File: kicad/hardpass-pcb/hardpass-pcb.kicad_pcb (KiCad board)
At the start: 2 copper layers, 30 x 65 mm, 27 parts, among them CON1 ER-OLED-FPC20, P1 Pi_Zero, SW1 1, SW10 C/UP, SW11 0/OK, SW12 OK/DN, SW2 2, SW3 3, SW4 4, SW5 5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

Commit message: added reset circuit to oled
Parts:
- added C7: 0.1µF, Capacitors_SMD:C_1206, B.Cu at (134.5, 88.2)
- added R2: 100k, Resistors_SMD:R_1206, B.Cu at (141.0, 88.2)
- added R3: 100k, Resistors_SMD:R_1206, B.Cu at (137.8, 88.2)
- moved C1 0.11 mm to (130.8, 104.0), turned to 270 degrees
- moved C2 0.11 mm to (146.2, 101.5), turned to 180 degrees
- moved R10 0.11 mm to (137.8, 93.5), turned to 90 degrees
- moved R11 0.10 mm to (141.0, 93.5), turned to 90 degrees
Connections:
- net Net-(CON1-Pad10) renamed /OLED_CS
- net Net-(CON1-Pad12) renamed /OLED_DC
- C1 pad 1: +3V3 -> GND
- C1 pad 2: GND -> +3V3
- C2 pad 1: +3V3 -> GND
- C2 pad 2: GND -> +3V3
- CON1 pad 11: Net-(CON1-Pad11) -> /OLED_RES
- R10 pad 1: +3V3 -> OLED_SCL
- R10 pad 2: OLED_SCL -> +3V3
- R11 pad 1: +3V3 -> OLED_SDA
- R11 pad 2: OLED_SDA -> +3V3
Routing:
- net /OLED_RES: track 0.00 -> 12.6 mm, vias 0 -> 2
- net Net-(C7-Pad1): track 0.00 -> 6.59 mm
- net +3V3: track 39.4 -> 39.5 mm, vias 6 -> 7

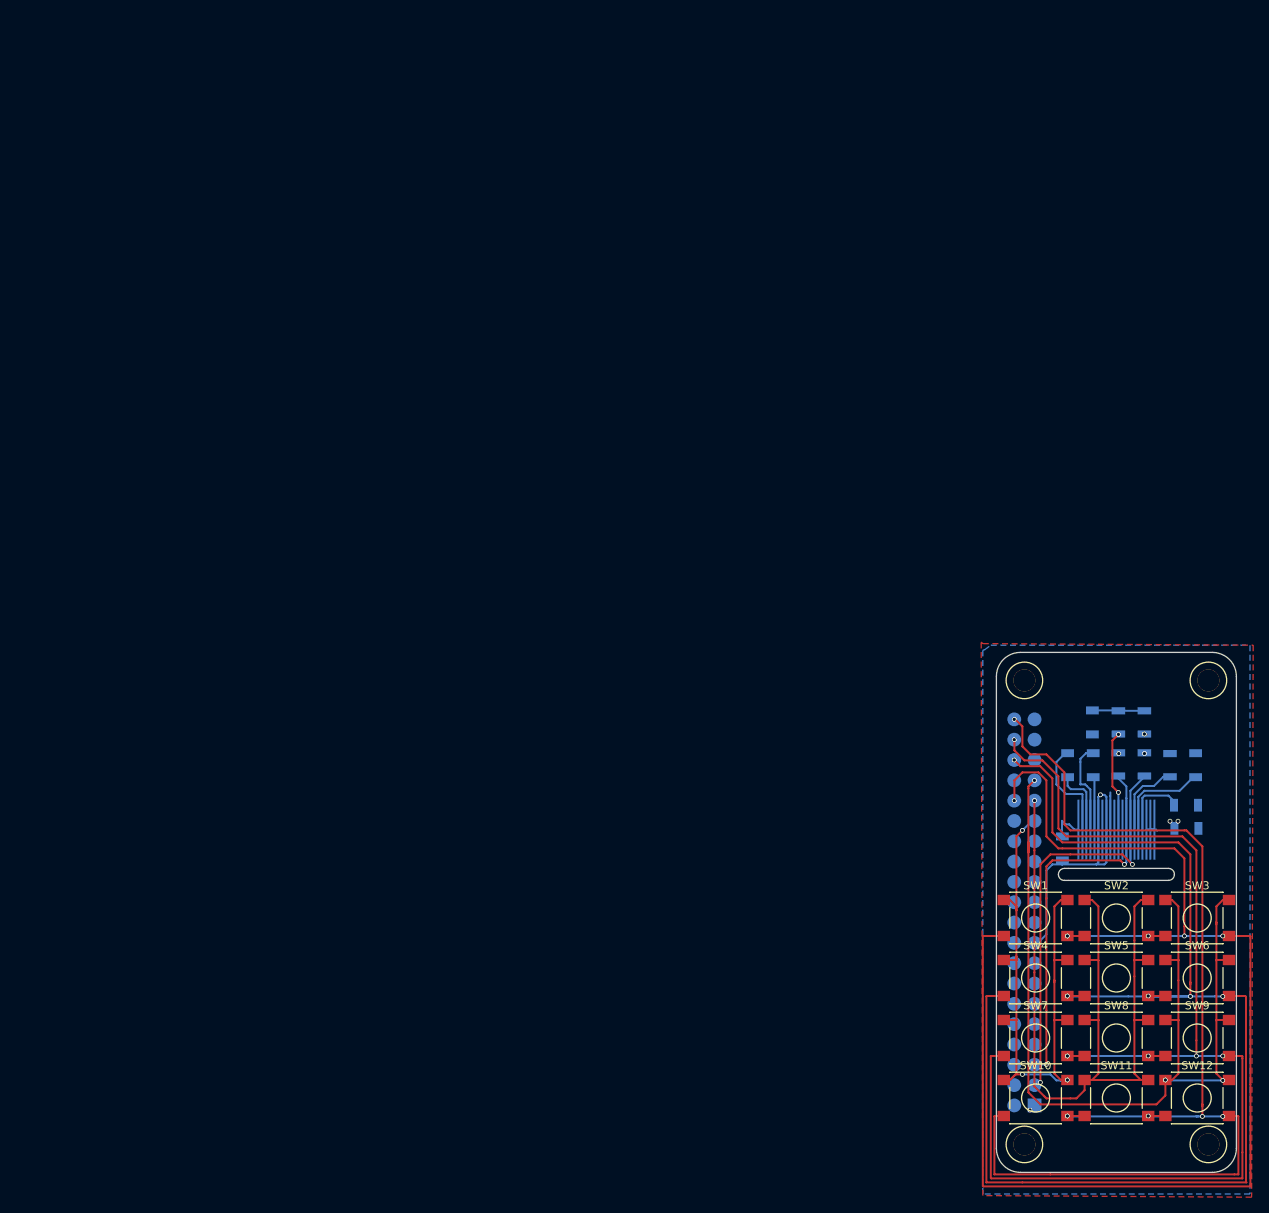
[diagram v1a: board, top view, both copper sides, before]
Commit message: re-done pcb for 30 pin oled
pcb was completely redone, fixing header-misalignment (hopefully) and removing ugly silk screen from the front
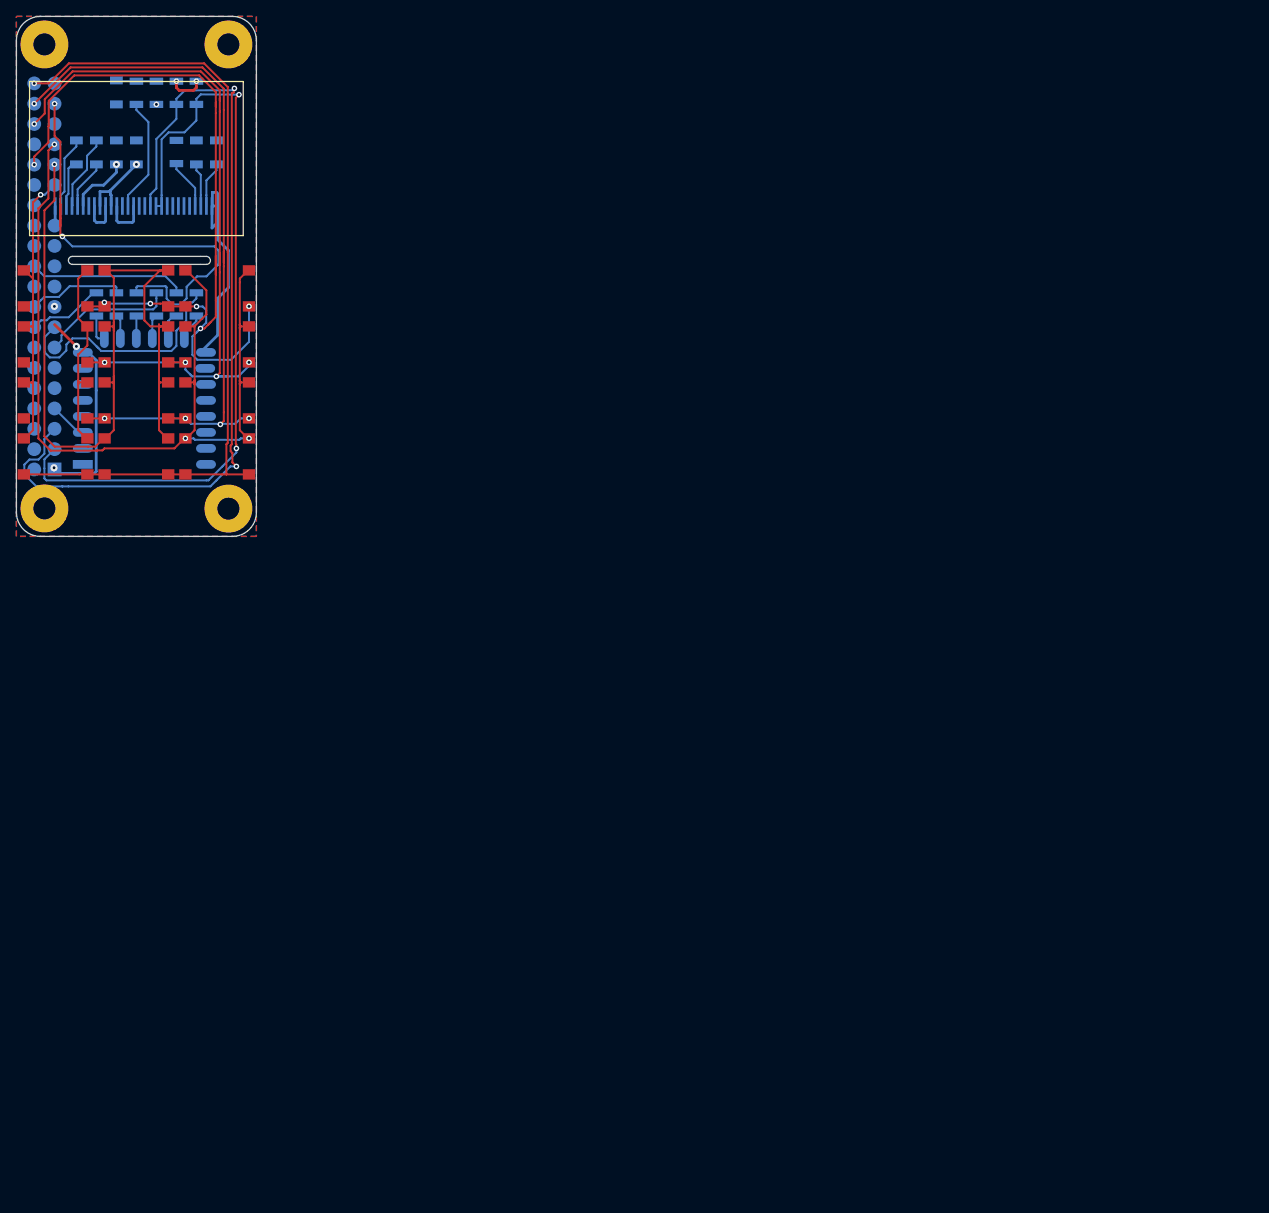
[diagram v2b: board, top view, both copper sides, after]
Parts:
- removed CON1: ER-OLED-FPC20, hardpass:Solderpads_OLED20Pin_.5mmPitch
- removed the REF** at (126.0, 83.0)
- removed the REF** at (149.0, 141.0)
- removed the REF** at (126.0, 141.0)
- removed the REF** at (149.0, 83.0)
- added P2: OLED_I2C, adafruit-oled:UG-2864HSWEG01_0.96IN_WRAPAROUND, F.Cu at (15.0, 22.5)
- added R12: 33, Resistors_SMD:R_1206, B.Cu at (10.0, 36.0)
- added R13: 33, Resistors_SMD:R_1206, B.Cu at (12.5, 36.0)
- added R14: 33, Resistors_SMD:R_1206, B.Cu at (15.0, 36.0)
- added R15: 33, Resistors_SMD:R_1206, B.Cu at (17.5, 36.0)
- added R16: 33, Resistors_SMD:R_1206, B.Cu at (20.0, 36.0)
- added R17: 33, Resistors_SMD:R_1206, B.Cu at (22.5, 36.0)
- added REF**: 1pin, hardpass:1pin_nosilk, F.Cu at (26.5, 61.5)
- added REF**: 1pin, hardpass:1pin_nosilk, F.Cu at (3.50, 61.5)
- added REF**: 1pin, hardpass:1pin_nosilk, F.Cu at (26.5, 3.50)
- added REF**: 1pin, hardpass:1pin_nosilk, F.Cu at (3.50, 3.50)
- added U2: ESP-12E, hardpass:ESP-12E_smd, B.Cu at (9.00, 56.0)
- P1: footprint hardpass:Pin_Header_Mirrored-NoHoles_2x20 -> hardpass:Pin_Header_Mirrored-NoHoles_centered_2x20
- SW1, SW10, SW11, SW12, SW2, SW3, SW4, SW5, SW6, SW7, SW8, SW9: footprint Buttons_Switches_SMD:SW_SPST_PTS645 -> hardpass:SW_SPST_PTS645_nosilk
- moved P1 159.6 mm to (3.50, 32.5)
- moved C2 156.1 mm to (15.0, 17.0), turned to 270 degrees
- moved C1 146.8 mm to (12.5, 17.0)
- moved C4 146.5 mm to (22.5, 17.0)
- moved R2 146.4 mm to (17.5, 9.55)
- moved SW10 146.4 mm to (4.90, 55.0)
- moved SW11 146.4 mm to (15.0, 55.0)
- moved SW12 146.4 mm to (25.1, 55.0)
- moved C5 146.3 mm to (10.0, 17.0)
- moved SW7 146.1 mm to (4.90, 48.0)
- moved SW8 146.1 mm to (15.0, 48.0)
- moved SW9 146.1 mm to (25.1, 48.0)
- moved C3 146.1 mm to (25.0, 17.0), turned to 90 degrees
- moved R1 145.9 mm to (20.0, 16.9)
- moved SW4 145.9 mm to (4.90, 41.0)
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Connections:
- R3 pad 1: /OLED_RES -> Net-(P2-Pad14)
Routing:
- net ROW_2: track 162.1 -> 92.1 mm
- net ROW_1: track 167.8 -> 101.6 mm, vias 5 -> 6
- net OLED_SCL: track 48.1 -> 106.8 mm
- net SD_D2: track 0.00 -> 57.4 mm, vias 0 -> 2
- net ROW_3: track 148.2 -> 93.4 mm
- net OLED_SDA: track 52.4 -> 97.4 mm
- net ROW_4: track 141.6 -> 103.6 mm, vias 5 -> 1
- net ESP_CLK: track 0.00 -> 30.9 mm
- net GND: track 12.1 -> 42.0 mm
- net SD_D1: track 0.00 -> 19.6 mm
- net SD_D3: track 0.00 -> 16.9 mm
- net Net-(P2-Pad14): track 0.00 -> 14.4 mm
- net COL_1: track 78.1 -> 64.5 mm, vias 3 -> 1
- net /OLED_RES: track 12.6 -> 0.00 mm, vias 2 -> 0
- net SD_D0: track 0.00 -> 12.1 mm
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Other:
- outline, holes or cut-outs redrawn
- net class Default: clearance 0.2 -> 0.25; via_dia 0.6 -> 0.7; via_drill 0.4 -> 0.35
- net class Power: clearance 0.2 -> 0.25; trace_width 0.45 -> 0.35; via_dia 0.6 -> 0.9; via_drill 0.4 -> 0.35
- rule pad_to_mask_clearance: 0.2 -> 0
- rule trace_clearance: 0.2 -> 0.25
- rule via_min_size: 0.4 -> 0.7

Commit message: added logo
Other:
- board text added: "hardpass 0.2.2"
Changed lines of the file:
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@@
     (links 107)
     (no_connects 7)
-    (area -0.050001 -0.050001 30.050001 65.050001)
+    (area -0.666014 -0.573 30.425001 65.655)
     (thickness 1.6)
-    (drawings 14)
+    (drawings 15)
     (tracks 547)
     (zones 0)
@@
       (net 1 GND))
   )
+  (gr_text "hardpass 0.2.2" (at 15 61.5) (layer F.SilkS)
+    (effects (font (size 1.5 1.5) (thickness 0.3)))
+  )
   (gr_line (start 23 30) (end 23.75 30) (layer Edge.Cuts) (width 0.1))

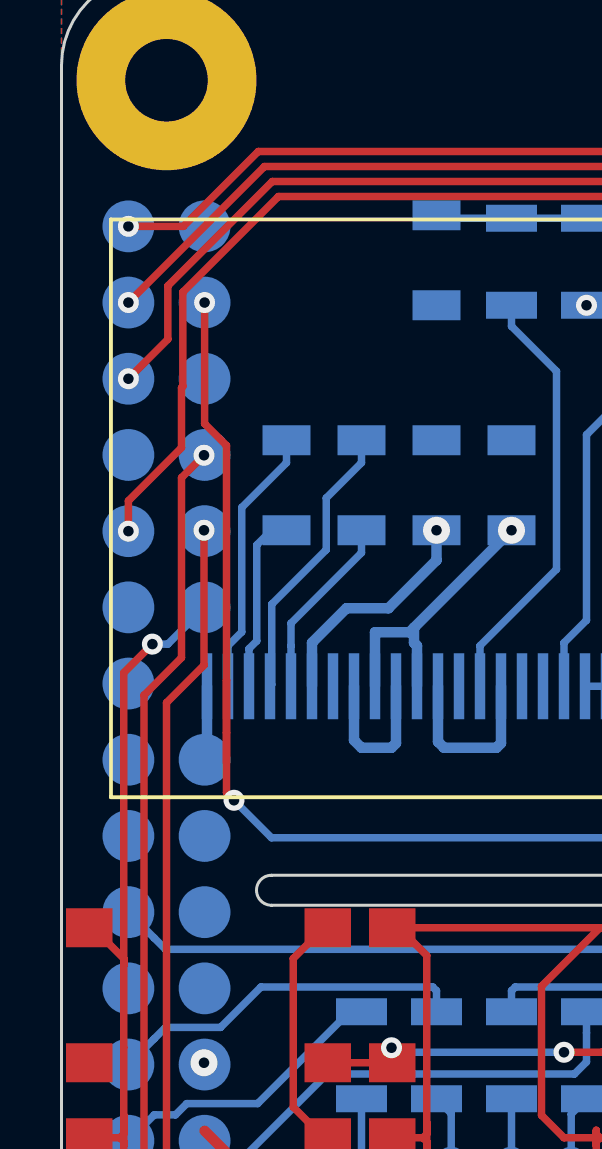
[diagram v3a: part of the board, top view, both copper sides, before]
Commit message: add tda8029 footprint
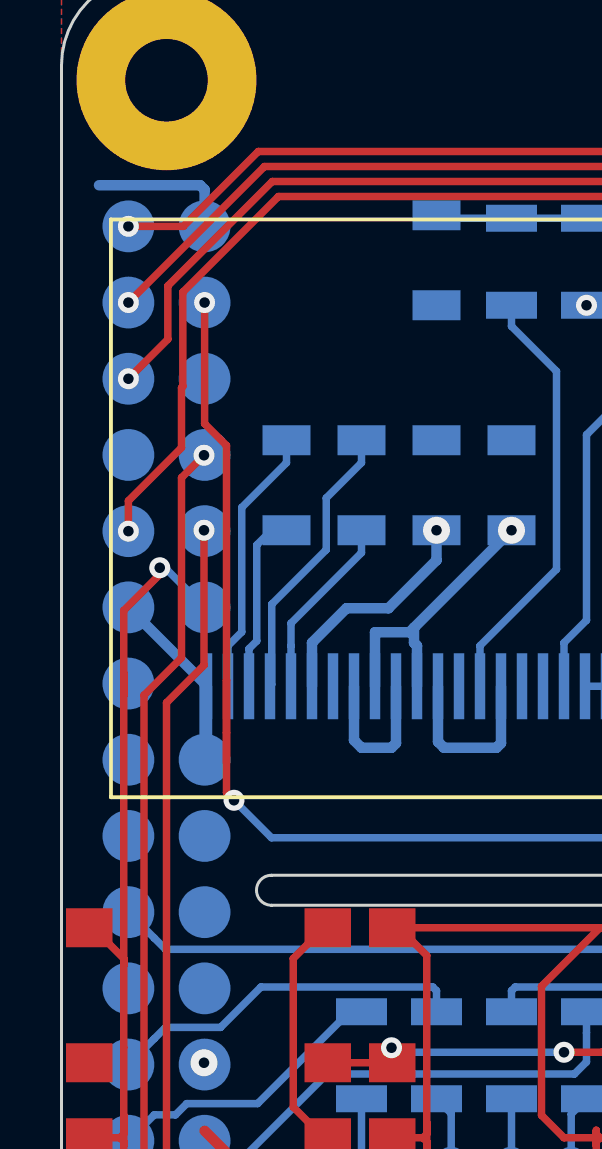
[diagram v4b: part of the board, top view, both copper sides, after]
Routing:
- net GND: track 42.0 -> 52.9 mm
- net COL_1: track 64.5 -> 67.7 mm
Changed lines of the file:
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@@
   (general
     (links 107)
-    (no_connects 7)
-    (area -0.666014 -0.573 30.425001 65.655)
+    (no_connects 6)
+    (area -0.050001 -0.050001 30.050001 65.050001)
     (thickness 1.6)
     (drawings 15)
-    (tracks 547)
+    (tracks 555)
     (zones 0)
     (modules 37)
@@
     (mod_text_size 1 1)
     (mod_text_width 0.15)
-    (pad_size 6 6)
-    (pad_drill 2.75)
+    (pad_size 1.7272 1.7272)
+    (pad_drill 0)
     (pad_to_mask_clearance 0)
     (aux_axis_origin 0 0)
-    (visible_elements FFFFFF7F)
+    (visible_elements FFFFEF7F)
     (pcbplotparams
       (layerselection 0x00030_80000001)
@@
     (add_net ESP_CHPD)
     (add_net ESP_CLK)
-    (add_net GND)
     (add_net "Net-(C3-Pad1)")
     (add_net "Net-(C4-Pad1)")
@@
     (uvia_drill 0.1)
     (add_net +3V3)
+    (add_net GND)
   )
   (module hardpass:1pin_nosilk (layer F.Cu)
@@
     (pad 22 smd oval (at 14 0) (size 2.5 1.1) (drill (offset 0.7 0)) (layers B.Cu B.Paste B.Mask)
       (net 59 "Net-(U2-Pad22)"))
-    (model ${ESPLIB}/ESP8266.3dshapes/ESP-12.wrl
-      (at (xyz 0.04 0 0))
+    (model /home/tobias/Desktop/30pin-hardpass/hardpass-passwordmanager/kicad/hardpass-pcb/kicad-ESP8266/ESP8266.3dshapes/ESP-12.wrl
+      (at (xyz 0 0 0))
       (scale (xyz 0.3937 0.3937 0.3937))
       (rotate (xyz 0 0 0))
@@
   (gr_arc (start 27 3) (end 27 0) (angle 90) (layer Edge.Cuts) (width 0.1))
   (gr_arc (start 3 3) (end 0 3) (angle 90) (layer Edge.Cuts) (width 0.1))
+  (segment (start 4.621014 7) (end 1.25 7) (width 0.35) (layer B.Cu) (net 1))
+  (segment (start 4.7697 8.37) (end 4.7697 7.148686) (width 0.35) (layer B.Cu) (net 1))
+  (segment (start 4.7697 7.148686) (end 4.621014 7) (width 0.35) (layer B.Cu) (net 1))
+  (segment (start 2.2297 21.07) (end 4.77 23.6103) (width 0.35) (layer B.Cu) (net 1))
+  (segment (start 4.77 23.6103) (end 4.77 26.15) (width 0.35) (layer B.Cu) (net 1))
   (segment (start 25.15 25.75) (end 25.15 27.9) (width 0.35) (layer B.Cu) (net 1))
   (segment (start 25.15 27.9) (end 26.5 29.25) (width 0.35) (layer B.Cu) (net 1))
@@
   (segment (start 3.468301 32.468601) (end 3.093299 32.093599) (width 0.25) (layer B.Cu) (net 25))
   (segment (start 3.093299 32.093599) (end 2.2297 31.23) (width 0.25) (layer B.Cu) (net 25))
+  (segment (start 3.275 19.75) (end 3.4497 19.75) (width 0.25) (layer B.Cu) (net 30))
+  (segment (start 3.4497 19.75) (end 4.7697 21.07) (width 0.25) (layer B.Cu) (net 30))
+  (segment (start 2.075001 21.174999) (end 3.275 19.975) (width 0.25) (layer F.Cu) (net 30))
+  (segment (start 3.275 19.975) (end 3.275 19.75) (width 0.25) (layer F.Cu) (net 30))
+  (via (at 3.275 19.75) (size 0.7) (drill 0.35) (layers F.Cu B.Cu) (net 30))
+  (segment (start 2.075001 24) (end 2.075001 23.250332) (width 0.25) (layer F.Cu) (net 30))
+  (segment (start 2.075001 33) (end 2.075001 24) (width 0.25) (layer F.Cu) (net 30))
+  (segment (start 2.075001 24) (end 2.075001 21.174999) (width 0.25) (layer F.Cu) (net 30))
   (segment (start 8.75 31.75) (end 7.724999 32.775001) (width 0.25) (layer F.Cu) (net 30))
   (segment (start 7.724999 32.775001) (end 7.724999 37.724999) (width 0.25) (layer F.Cu) (net 30))
@@
   (segment (start 7.724999 42.25) (end 7.724999 45.5) (width 0.25) (layer F.Cu) (net 30))
   (segment (start 7.724999 42.25) (end 7.75 42.25) (width 0.25) (layer F.Cu) (net 30))
-  (segment (start 3.029754 22.295579) (end 3.544121 22.295579) (width 0.25) (layer B.Cu) (net 30))
-  (segment (start 3.544121 22.295579) (end 4.7697 21.07) (width 0.25) (layer B.Cu) (net 30))
   (segment (start 2.075001 33) (end 2.075001 35.75) (width 0.25) (layer F.Cu) (net 30))
   (segment (start 2.075001 32.775001) (end 2.075001 33) (width 0.25) (layer F.Cu) (net 30))
-  (segment (start 2.075001 33) (end 2.075001 23.250332) (width 0.25) (layer F.Cu) (net 30))
-  (segment (start 2.075001 23.250332) (end 3.029754 22.295579) (width 0.25) (layer F.Cu) (net 30))
-  (via (at 3.029754 22.295579) (size 0.7) (drill 0.35) (layers F.Cu B.Cu) (net 30))
   (segment (start 8.875 31.75) (end 8.75 31.75) (width 0.25) (layer F.Cu) (net 30))
   (segment (start 2.075001 35.75) (end 2.075001 38) (width 0.25) (layer F.Cu) (net 30))

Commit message: routed 2nd board
not finished, but a start
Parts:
- added C10: 100pF, Capacitors_SMD:C_1206, F.Cu at (88.2, 31.8)
- added C11: 10µF, Capacitors_SMD:C_1206, F.Cu at (75.5, 41.8)
- added C12: 100nF, Capacitors_SMD:C_1206, F.Cu at (75.5, 44.2)
- added C13: 22nF, Capacitors_SMD:C_1206, F.Cu at (76.5, 37.5)
- added C14: 100pF, Capacitors_SMD:C_1206, F.Cu at (75.5, 26.0)
- added C15: 22pF, Capacitors_SMD:C_1206, F.Cu at (69.2, 51.5)
- added C16: 220nF, Capacitors_SMD:C_1206, F.Cu at (69.0, 30.2)
- added C17: 22pF, Capacitors_SMD:C_1206, F.Cu at (62.2, 51.5)
- added C18: 100nF, Capacitors_SMD:C_1206, F.Cu at (59.2, 40.5)
- added C19: 10µF, Capacitors_SMD:C_1206, F.Cu at (88.0, 40.0)
- added C20: 220nF, Capacitors_SMD:C_1206, F.Cu at (61.0, 30.5)
- added C21: 220nF, Capacitors_SMD:C_1206, F.Cu at (61.0, 27.8)
- added C8: 220nF, Capacitors_SMD:C_1206, F.Cu at (75.5, 28.5)
- added C9: 33pF, Capacitors_SMD:C_1206, F.Cu at (75.5, 31.0)
- added P3: Pi_Zero, hardpass:Pin_Header_Straight_2x20_Pitch2.54mm_centered, F.Cu at (53.5, 32.5)
- added R4: 100, Resistors_SMD:R_1206, F.Cu at (69.0, 27.2)
- added R5: 180, Resistors_SMD:R_1206, F.Cu at (75.5, 33.5)
- added REF**: 1pin, hardpass:1pin_nosilk, F.Cu at (76.5, 61.5)
- added REF**: 1pin, hardpass:1pin_nosilk, F.Cu at (76.5, 3.50)
- added REF**: 1pin, hardpass:1pin_nosilk, F.Cu at (53.5, 3.50)
- added REF**: 1pin, hardpass:1pin_nosilk, F.Cu at (53.5, 61.5)
- added U1: ISO7816, hardpass:CAF99-08153-S132, F.Cu at (66.2, 16.0)
- added U3: TDA8029, Housings_QFP:LQFP-32_7x7mm_Pitch0.8mm, F.Cu at (67.0, 37.5)
- added Y1: 14.745MHz, Crystals:Crystal_HC49-U_Vertical, F.Cu at (68.2, 47.5)
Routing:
- net Net-(R5-Pad1): track 0.00 -> 38.5 mm
- net Net-(C14-Pad2): track 0.00 -> 34.9 mm
- net CARD_RX: track 0.00 -> 33.0 mm
- net CARD_TX: track 0.00 -> 31.3 mm
- net +5V: track 0.00 -> 23.3 mm
- net Net-(C9-Pad1): track 0.00 -> 13.3 mm
- net Net-(C21-Pad1): track 0.00 -> 11.2 mm
- net Net-(C15-Pad2): track 0.00 -> 11.0 mm
- net Net-(C17-Pad2): track 0.00 -> 10.6 mm
- net Net-(C10-Pad2): track 0.00 -> 10.0 mm
- net GND: track 52.9 -> 62.5 mm, vias 0 -> 17
- net Net-(C21-Pad2): track 0.00 -> 6.87 mm
- net Net-(C13-Pad1): track 0.00 -> 6.29 mm
- net Net-(C20-Pad1): track 0.00 -> 5.55 mm
- net Net-(R4-Pad1): track 0.00 -> 4.75 mm
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- added copper zone on F.Cu, net +5V
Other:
- board size 30 x 65 mm -> 80 x 65 mm
